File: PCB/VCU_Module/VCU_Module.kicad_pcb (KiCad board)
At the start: 2 copper layers, 85.2 x 107.8 mm, 66 parts, among them IC1 STM32C092RCT6, J1 5810132011, J10 12V, J11 Conn_ST_STDC14, J12 MCU1, J13 MCU2, J14 5V, J15 3V3, J16 MCU3, J17 MCU4, J2 CN1, J3 CN2, J4 CN3, J5 MCU6, J6 CN4, J7 MCU5, J8 Termination Resistor Jumper, J9 GND, Q1 PJD9P06A-AU_L2_000A1, SW2 SW_Push, U3 LMR33640DDDA, U4 LMR33640DDDA, U6 MCP2562FDT-H_SN

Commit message: move STLink connector and change component to correct version with alignment tabs
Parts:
- moved J11 41.0 mm to (156.0, 128.4), turned to 90 degrees
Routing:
- net /MCU/NRST: track 51.6 -> 68.6 mm, vias 1 -> 2
- net /MCU/VCP_RX: track 38.4 -> 25.9 mm
- net /MCU/VCP_TX: track 34.2 -> 24.2 mm
- net /MCU/SWCLK/BOOT0: track 34.1 -> 43.7 mm
- net /MCU/SWO: track 26.9 -> 35.6 mm
- net /MCU/SWDIO: track 35.0 -> 43.5 mm
- net 3V3: track 152.7 -> 150.8 mm

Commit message: move stdc14 connector reroute traces fix drc and schematic parity issues rerun make for build files
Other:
- board text added: "${TITLE} ${COMPANY} REV ${REVISION} ${ISSUE_DATE}"
- board text added: "CAN H CAN H CAN L CAN L"
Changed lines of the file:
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@@
 	(paper "A4")
 	(title_block
-		(title "BATTERY MANAGEMENT UNIT (BMU)")
-		(date "2026-05-14")
+		(title "VEHICLE CONTROL UNIT (VCU) Dev Board")
+		(date "2026-08-13")
 		(rev "1.0")
 		(company "VIKING MOTOR SPORTS (VMS)")
@@
 		(sheetname "/MCU/")
 		(sheetfile "MCU.kicad_sch")
+		(units
+			(unit
+				(name "A")
+				(pins "1" "4" "8" "2" "3" "5" "6" "7")
+			)
+		)
 		(attr smd)
 		(duplicate_pad_numbers_are_jumpers no)
@@
 		(sheetname "/")
 		(sheetfile "VCU_Module.kicad_sch")
+		(units
+			(unit
+				(name "A")
+				(pins "2" "3" "6" "1" "9" "7" "8" "5" "4")
+			)
+		)
 		(attr smd)
 		(duplicate_pad_numbers_are_jumpers no)
@@
 		)
 		(property "Value" "3V3"
-			(at 0 10 0)
-			(layer "F.Fab")
+			(at 3.1 4.31 0)
+			(layer "F.SilkS")
 			(effects
 				(font
@@
 		)
 		(property "Value" "5V"
-			(at 0 10 0)
-			(layer "F.Fab")
+			(at 2.85 3.21 0)
+			(layer "F.SilkS")
 			(effects
 				(font
@@
 			)
 		)
-		(property "Datasheet" "https://www.st.com/content/ccc/resource/technical/document/user_manual/group1/99/49/91/b6/b2/3a/46/e5/DM00526767/files/DM00526767.pdf/jcr:content/translations/en.DM00526767.pdf"
+		(property "Datasheet" "https://suddendocs.samtec.com/catalog_english/ftsh_th.pdf"
 			(at 0 0 90)
 			(layer "F.Fab")
@@
 			)
 		)
-		(property "DPN" "612-FTSH-107-01-F-DV-K-ND"
+		(property "DPN" "SAM12420-ND"
 			(at 0 0 90)
 			(unlocked yes)
@@
 			)
 		)
-		(property "MPN" "FTSH-107-01-F-DV-K"
+		(property "MPN" "FTSH-107-01-S-D-K"
 			(at 0 0 90)
 			(unlocked yes)
@@
 			)
 		)
-		(property "Purchase Link" "https://www.digikey.com/en/products/detail/samtec-inc/FTSH-107-01-F-DV-K/2650001"
+		(property "Purchase Link" "https://www.digikey.com/en/products/detail/samtec-inc/FTSH-107-01-S-D-K/2650004?gclsrc=aw.ds&gad_source=1&gad_campaignid=17336967819&gbraid=0AAAAADrbLlicyKK0eY_V0wleFKoDjVbWz&gclid=CjwKCAjw1vXTBhB-EiwAEKr_k6pgiYkH2W21gU4f999biLNDO9FzNBRms_SrUikYiU-KfRn2oXJkshoCrk8QAvD_BwE"
 			(at 0 0 90)
 			(unlocked yes)
@@
 			)
 		)
+		(property "MFR" "Samtec Inc."
+			(at 0 0 90)
+			(unlocked yes)
+			(layer "F.Fab")
+			(hide yes)
+			(effects
+				(font
+					(size 1 1)
+					(thickness 0.15)
+				)
+			)
+		)
 		(property ki_fp_filters "PinHeader?2x07?P1.27mm*")
 		(sheetname "/MCU/")
 		(sheetfile "MCU.kicad_sch")
+		(units
+			(unit
+				(name "A")
+				(pins "1" "2" "11" "3" "5" "7" "12" "6" "4" "8" "10" "9" "13" "14")
+			)
+		)
 		(attr through_hole)
 		(duplicate_pad_numbers_are_jumpers no)
@@
 		(sheetname "/MCU/")
 		(sheetfile "MCU.kicad_sch")
+		(units
+			(unit
+				(name "A")
+				(pins "1" "2" "3")
+			)
+		)
 		(attr smd)
 		(duplicate_pad_numbers_are_jumpers no)
@@
 		(sheetname "/MCU/")
 		(sheetfile "MCU.kicad_sch")
+		(units
+			(unit
+				(name "A")
+				(pins "10" "11" "12" "6" "17" "18" "19" "20" "21" "22" "23" "24" "36"
+					"37" "42" "43" "44" "45" "46" "47" "50" "51" "52" "53" "54" "55" "56"
+					"40" "41" "7" "9" "8" "35" "34" "33" "32" "31" "30" "63" "62" "61" "60"
+					"59" "58" "57" "29" "28" "27" "5" "4" "3" "2" "1" "64" "49" "48" "39"
+					"38" "26" "25" "16" "15" "14" "13"
+				)
+			)
+		)
 		(attr smd)
 		(duplicate_pad_numbers_are_jumpers no)
@@
 		(sheetname "/")
 		(sheetfile "VCU_Module.kicad_sch")
+		(units
+			(unit
+				(name "A")
+				(pins "2" "3" "6" "1" "9" "7" "8" "5" "4")
+			)
+		)
 		(attr smd)
 		(duplicate_pad_numbers_are_jumpers no)
@@
 		(sheetname "/")
 		(sheetfile "VCU_Module.kicad_sch")
+		(units
+			(unit
+				(name "A")
+				(pins "1" "3" "2" "4")
+			)
+		)
 		(attr through_hole)
 		(duplicate_pad_numbers_are_jumpers no)
@@
 		(sheetname "/")
 		(sheetfile "VCU_Module.kicad_sch")
+		(units
+			(unit
+				(name "A")
+				(pins "1" "2")
+			)
+		)
 		(attr smd)
 		(duplicate_pad_numbers_are_jumpers no)
@@
 		(sheetname "/")
 		(sheetfile "VCU_Module.kicad_sch")
+		(units
+			(unit
+				(name "A")
+				(pins "A1" "A2" "A3" "A4" "A5" "A6" "A7" "A8" "A9" "A10" "A11" "A12"
+					"A13" "A14" "A15" "A16" "A17" "A18" "A19" "A20"
+				)
+			)
+			(unit
+				(name "B")
+				(pins "B1" "B2" "B3" "B4" "B5" "B6" "B7" "B8" "B9" "B10" "B11" "B12")
+			)
+		)
 		(attr through_hole)
 		(duplicate_pad_numbers_are_jumpers no)
@@
 		(layer "Edge.Cuts")
 	)
+	(gr_text "CAN H\n\nCAN H\n\nCAN L\n\nCAN L"
+		(at 146.5 130.6 0)
+		(layer "F.SilkS")
+		(effects
+			(font
+				(size 0.79 0.5)
+				(thickness 0.125)
+			)
+			(justify left bottom)
+		)
+	)
 	(gr_text "PC10\n\nPC11\n\nPC12\n\nPC13\n\nPC14\n\nPC15\n\nPC0\n\nPC1\n\nPC2\n\nPC3"
 		(at 157.25 120.25 0)
@@
 				(thickness 0.125)
 			)
+			(justify left bottom)
+		)
+	)
+	(gr_text "${TITLE}\n${COMPANY}\nREV ${REVISION}\n${ISSUE_DATE}"
+		(at 116.5 154.5 0)
+		(layer "F.SilkS")
+		(effects
+			(font
+				(size 1 1)
+				(thickness 0.125)
+			)

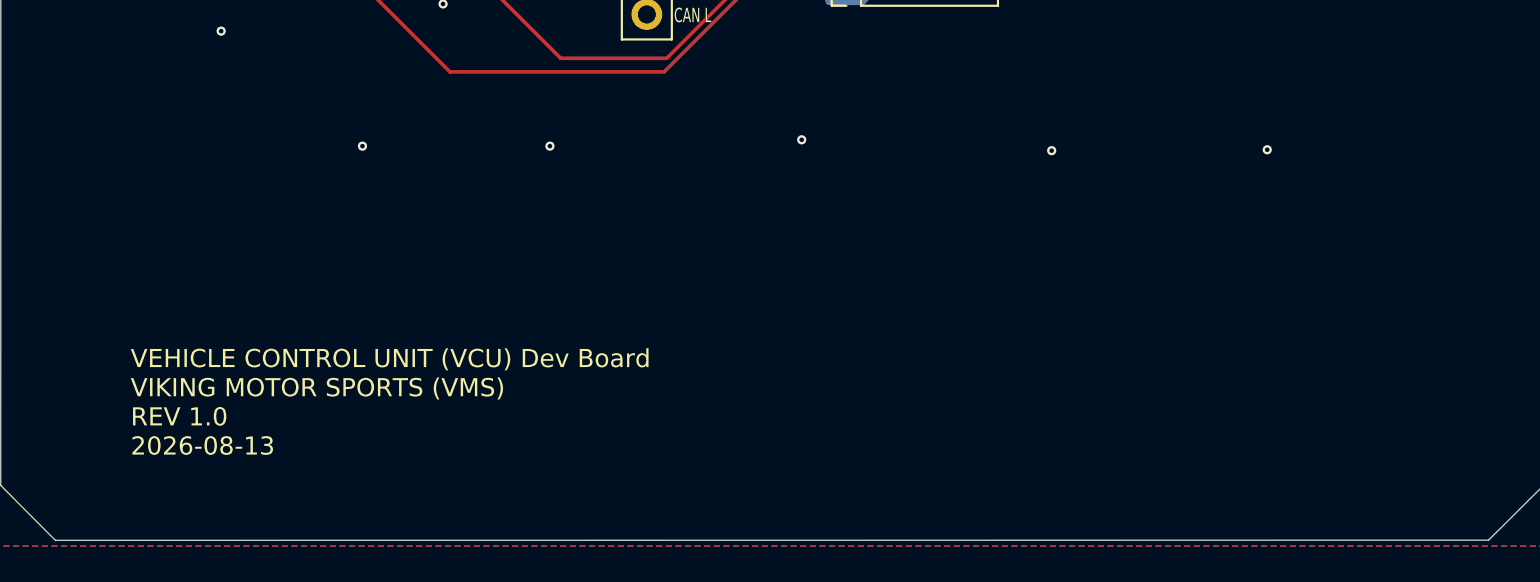
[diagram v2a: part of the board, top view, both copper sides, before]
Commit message: Add perfboard to allow placement of additional components
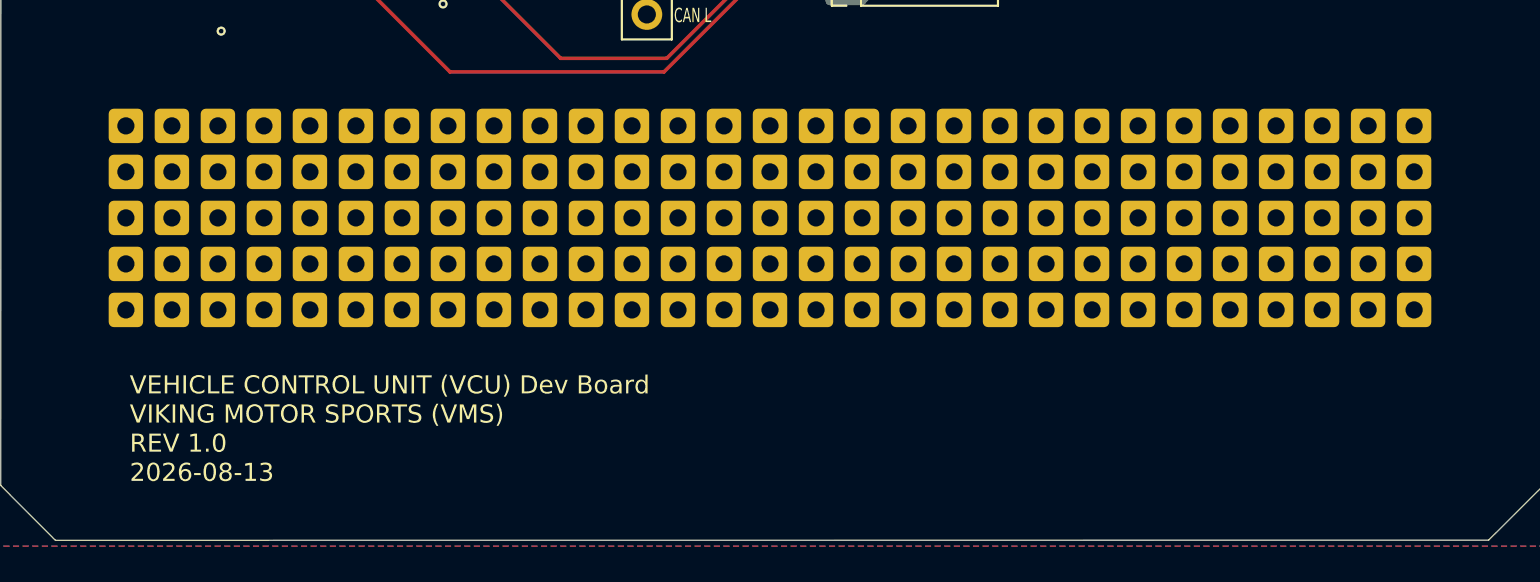
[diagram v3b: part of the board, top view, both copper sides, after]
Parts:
- added REF**: perf_hole, VMS_Footprints:perf_hole, F.Cu at (123.9, 136.2)
- added REF**: perf_hole, VMS_Footprints:perf_hole, F.Cu at (164.5, 138.8)
- added REF**: perf_hole, VMS_Footprints:perf_hole, F.Cu at (146.7, 146.4)
- added REF**: perf_hole, VMS_Footprints:perf_hole, F.Cu at (156.9, 143.9)
- added REF**: perf_hole, VMS_Footprints:perf_hole, F.Cu at (172.1, 136.2)
- added REF**: perf_hole, VMS_Footprints:perf_hole, F.Cu at (151.8, 136.2)
- added REF**: perf_hole, VMS_Footprints:perf_hole, F.Cu at (184.8, 136.2)
- added REF**: perf_hole, VMS_Footprints:perf_hole, F.Cu at (118.8, 143.9)
- added REF**: perf_hole, VMS_Footprints:perf_hole, F.Cu at (167.0, 146.4)
- added REF**: perf_hole, VMS_Footprints:perf_hole, F.Cu at (164.5, 146.4)
- added REF**: perf_hole, VMS_Footprints:perf_hole, F.Cu at (144.2, 136.2)
- added REF**: perf_hole, VMS_Footprints:perf_hole, F.Cu at (121.3, 136.2)
- added REF**: perf_hole, VMS_Footprints:perf_hole, F.Cu at (126.4, 138.8)
- added REF**: perf_hole, VMS_Footprints:perf_hole, F.Cu at (141.6, 146.4)
- added REF**: perf_hole, VMS_Footprints:perf_hole, F.Cu at (139.1, 141.3)
- added REF**: perf_hole, VMS_Footprints:perf_hole, F.Cu at (159.4, 143.9)
- added REF**: perf_hole, VMS_Footprints:perf_hole, F.Cu at (182.3, 146.4)
- added REF**: perf_hole, VMS_Footprints:perf_hole, F.Cu at (139.1, 138.8)
- added REF**: perf_hole, VMS_Footprints:perf_hole, F.Cu at (139.1, 146.4)
- added REF**: perf_hole, VMS_Footprints:perf_hole, F.Cu at (121.3, 141.3)
- added REF**: perf_hole, VMS_Footprints:perf_hole, F.Cu at (131.5, 146.4)
- added REF**: perf_hole, VMS_Footprints:perf_hole, F.Cu at (172.1, 143.9)
- added REF**: perf_hole, VMS_Footprints:perf_hole, F.Cu at (167.0, 143.9)
- added REF**: perf_hole, VMS_Footprints:perf_hole, F.Cu at (162.0, 141.3)
- added REF**: perf_hole, VMS_Footprints:perf_hole, F.Cu at (179.7, 138.8)
- added REF**: perf_hole, VMS_Footprints:perf_hole, F.Cu at (187.4, 143.9)
- added REF**: perf_hole, VMS_Footprints:perf_hole, F.Cu at (134.0, 146.4)
- added REF**: perf_hole, VMS_Footprints:perf_hole, F.Cu at (182.3, 143.9)
- added REF**: perf_hole, VMS_Footprints:perf_hole, F.Cu at (149.3, 136.2)
- added REF**: perf_hole, VMS_Footprints:perf_hole, F.Cu at (162.0, 138.8)
- added REF**: perf_hole, VMS_Footprints:perf_hole, F.Cu at (126.4, 141.3)
- added REF**: perf_hole, VMS_Footprints:perf_hole, F.Cu at (121.3, 146.4)
- added REF**: perf_hole, VMS_Footprints:perf_hole, F.Cu at (169.6, 141.3)
- added REF**: perf_hole, VMS_Footprints:perf_hole, F.Cu at (126.4, 136.2)
- added REF**: perf_hole, VMS_Footprints:perf_hole, F.Cu at (159.4, 138.8)
- added REF**: perf_hole, VMS_Footprints:perf_hole, F.Cu at (139.1, 143.9)
- added REF**: perf_hole, VMS_Footprints:perf_hole, F.Cu at (146.7, 141.3)
- added REF**: perf_hole, VMS_Footprints:perf_hole, F.Cu at (118.8, 141.3)
- added REF**: perf_hole, VMS_Footprints:perf_hole, F.Cu at (151.8, 141.3)
- added REF**: perf_hole, VMS_Footprints:perf_hole, F.Cu at (172.1, 138.8)
- added REF**: perf_hole, VMS_Footprints:perf_hole, F.Cu at (128.9, 141.3)
- added REF**: perf_hole, VMS_Footprints:perf_hole, F.Cu at (164.5, 141.3)
- added REF**: perf_hole, VMS_Footprints:perf_hole, F.Cu at (118.8, 146.4)
- added REF**: perf_hole, VMS_Footprints:perf_hole, F.Cu at (146.7, 136.2)
- added REF**: perf_hole, VMS_Footprints:perf_hole, F.Cu at (126.4, 143.9)
- added REF**: perf_hole, VMS_Footprints:perf_hole, F.Cu at (159.4, 146.4)
- added REF**: perf_hole, VMS_Footprints:perf_hole, F.Cu at (128.9, 146.4)
- added REF**: perf_hole, VMS_Footprints:perf_hole, F.Cu at (144.2, 138.8)
- added REF**: perf_hole, VMS_Footprints:perf_hole, F.Cu at (182.3, 138.8)
- added REF**: perf_hole, VMS_Footprints:perf_hole, F.Cu at (154.3, 143.9)
- added REF**: perf_hole, VMS_Footprints:perf_hole, F.Cu at (141.6, 136.2)
- added REF**: perf_hole, VMS_Footprints:perf_hole, F.Cu at (151.8, 143.9)
- added REF**: perf_hole, VMS_Footprints:perf_hole, F.Cu at (116.2, 146.4)
- added REF**: perf_hole, VMS_Footprints:perf_hole, F.Cu at (134.0, 143.9)
- added REF**: perf_hole, VMS_Footprints:perf_hole, F.Cu at (179.7, 141.3)
- added REF**: perf_hole, VMS_Footprints:perf_hole, F.Cu at (184.8, 138.8)
- added REF**: perf_hole, VMS_Footprints:perf_hole, F.Cu at (118.8, 136.2)
- added REF**: perf_hole, VMS_Footprints:perf_hole, F.Cu at (141.6, 141.3)
- added REF**: perf_hole, VMS_Footprints:perf_hole, F.Cu at (123.9, 146.4)
- added REF**: perf_hole, VMS_Footprints:perf_hole, F.Cu at (149.3, 141.3)
- added REF**: perf_hole, VMS_Footprints:perf_hole, F.Cu at (149.3, 146.4)
- added REF**: perf_hole, VMS_Footprints:perf_hole, F.Cu at (174.7, 138.8)
- added REF**: perf_hole, VMS_Footprints:perf_hole, F.Cu at (134.0, 136.2)
- added REF**: perf_hole, VMS_Footprints:perf_hole, F.Cu at (151.8, 138.8)
- added REF**: perf_hole, VMS_Footprints:perf_hole, F.Cu at (136.6, 146.4)
- added REF**: perf_hole, VMS_Footprints:perf_hole, F.Cu at (167.0, 141.3)
- added REF**: perf_hole, VMS_Footprints:perf_hole, F.Cu at (169.6, 136.2)
- added REF**: perf_hole, VMS_Footprints:perf_hole, F.Cu at (131.5, 136.2)
- added REF**: perf_hole, VMS_Footprints:perf_hole, F.Cu at (128.9, 143.9)
- added REF**: perf_hole, VMS_Footprints:perf_hole, F.Cu at (177.2, 141.3)
- added REF**: perf_hole, VMS_Footprints:perf_hole, F.Cu at (131.5, 143.9)
- added REF**: perf_hole, VMS_Footprints:perf_hole, F.Cu at (144.2, 141.3)
- added REF**: perf_hole, VMS_Footprints:perf_hole, F.Cu at (116.2, 136.2)
- added REF**: perf_hole, VMS_Footprints:perf_hole, F.Cu at (162.0, 143.9)
- added REF**: perf_hole, VMS_Footprints:perf_hole, F.Cu at (121.3, 143.9)
- added REF**: perf_hole, VMS_Footprints:perf_hole, F.Cu at (116.2, 138.8)
- added REF**: perf_hole, VMS_Footprints:perf_hole, F.Cu at (156.9, 141.3)
- added REF**: perf_hole, VMS_Footprints:perf_hole, F.Cu at (167.0, 136.2)
- added REF**: perf_hole, VMS_Footprints:perf_hole, F.Cu at (184.8, 141.3)
- added REF**: perf_hole, VMS_Footprints:perf_hole, F.Cu at (174.7, 141.3)
- added REF**: perf_hole, VMS_Footprints:perf_hole, F.Cu at (146.7, 138.8)
- added REF**: perf_hole, VMS_Footprints:perf_hole, F.Cu at (179.7, 146.4)
- added REF**: perf_hole, VMS_Footprints:perf_hole, F.Cu at (149.3, 138.8)
- added REF**: perf_hole, VMS_Footprints:perf_hole, F.Cu at (179.7, 136.2)
- added REF**: perf_hole, VMS_Footprints:perf_hole, F.Cu at (156.9, 136.2)
- added REF**: perf_hole, VMS_Footprints:perf_hole, F.Cu at (174.7, 143.9)
- added REF**: perf_hole, VMS_Footprints:perf_hole, F.Cu at (136.6, 141.3)
- added REF**: perf_hole, VMS_Footprints:perf_hole, F.Cu at (154.3, 141.3)
- added REF**: perf_hole, VMS_Footprints:perf_hole, F.Cu at (179.7, 143.9)
- added REF**: perf_hole, VMS_Footprints:perf_hole, F.Cu at (128.9, 136.2)
- added REF**: perf_hole, VMS_Footprints:perf_hole, F.Cu at (156.9, 146.4)
- added REF**: perf_hole, VMS_Footprints:perf_hole, F.Cu at (136.6, 138.8)
- added REF**: perf_hole, VMS_Footprints:perf_hole, F.Cu at (151.8, 146.4)
- added REF**: perf_hole, VMS_Footprints:perf_hole, F.Cu at (141.6, 143.9)
- added REF**: perf_hole, VMS_Footprints:perf_hole, F.Cu at (177.2, 143.9)
- added REF**: perf_hole, VMS_Footprints:perf_hole, F.Cu at (154.3, 138.8)
- added REF**: perf_hole, VMS_Footprints:perf_hole, F.Cu at (136.6, 136.2)
- added REF**: perf_hole, VMS_Footprints:perf_hole, F.Cu at (146.7, 143.9)
- added REF**: perf_hole, VMS_Footprints:perf_hole, F.Cu at (126.4, 146.4)
- added REF**: perf_hole, VMS_Footprints:perf_hole, F.Cu at (182.3, 136.2)
- added REF**: perf_hole, VMS_Footprints:perf_hole, F.Cu at (131.5, 138.8)
- added REF**: perf_hole, VMS_Footprints:perf_hole, F.Cu at (162.0, 146.4)
- added REF**: perf_hole, VMS_Footprints:perf_hole, F.Cu at (159.4, 136.2)
- added REF**: perf_hole, VMS_Footprints:perf_hole, F.Cu at (172.1, 141.3)
- added REF**: perf_hole, VMS_Footprints:perf_hole, F.Cu at (116.2, 141.3)
- added REF**: perf_hole, VMS_Footprints:perf_hole, F.Cu at (134.0, 138.8)
- added REF**: perf_hole, VMS_Footprints:perf_hole, F.Cu at (116.2, 143.9)
- added REF**: perf_hole, VMS_Footprints:perf_hole, F.Cu at (177.2, 146.4)
- added REF**: perf_hole, VMS_Footprints:perf_hole, F.Cu at (187.4, 138.8)
- added REF**: perf_hole, VMS_Footprints:perf_hole, F.Cu at (167.0, 138.8)
- added REF**: perf_hole, VMS_Footprints:perf_hole, F.Cu at (169.6, 138.8)
- added REF**: perf_hole, VMS_Footprints:perf_hole, F.Cu at (177.2, 138.8)
- added REF**: perf_hole, VMS_Footprints:perf_hole, F.Cu at (131.5, 141.3)
- added REF**: perf_hole, VMS_Footprints:perf_hole, F.Cu at (182.3, 141.3)
- added REF**: perf_hole, VMS_Footprints:perf_hole, F.Cu at (149.3, 143.9)
- added REF**: perf_hole, VMS_Footprints:perf_hole, F.Cu at (187.4, 146.4)
- added REF**: perf_hole, VMS_Footprints:perf_hole, F.Cu at (159.4, 141.3)
- added REF**: perf_hole, VMS_Footprints:perf_hole, F.Cu at (154.3, 146.4)
- added REF**: perf_hole, VMS_Footprints:perf_hole, F.Cu at (123.9, 143.9)
- added REF**: perf_hole, VMS_Footprints:perf_hole, F.Cu at (172.1, 146.4)
- added REF**: perf_hole, VMS_Footprints:perf_hole, F.Cu at (128.9, 138.8)
- added REF**: perf_hole, VMS_Footprints:perf_hole, F.Cu at (164.5, 136.2)
- added REF**: perf_hole, VMS_Footprints:perf_hole, F.Cu at (144.2, 146.4)
- added REF**: perf_hole, VMS_Footprints:perf_hole, F.Cu at (144.2, 143.9)
- added REF**: perf_hole, VMS_Footprints:perf_hole, F.Cu at (162.0, 136.2)
- added REF**: perf_hole, VMS_Footprints:perf_hole, F.Cu at (139.1, 136.2)
- added REF**: perf_hole, VMS_Footprints:perf_hole, F.Cu at (123.9, 141.3)
- added REF**: perf_hole, VMS_Footprints:perf_hole, F.Cu at (184.8, 143.9)
- added REF**: perf_hole, VMS_Footprints:perf_hole, F.Cu at (164.5, 143.9)
- added REF**: perf_hole, VMS_Footprints:perf_hole, F.Cu at (156.9, 138.8)
- added REF**: perf_hole, VMS_Footprints:perf_hole, F.Cu at (118.8, 138.8)
- added REF**: perf_hole, VMS_Footprints:perf_hole, F.Cu at (169.6, 146.4)
- added REF**: perf_hole, VMS_Footprints:perf_hole, F.Cu at (154.3, 136.2)
- added REF**: perf_hole, VMS_Footprints:perf_hole, F.Cu at (136.6, 143.9)
- added REF**: perf_hole, VMS_Footprints:perf_hole, F.Cu at (177.2, 136.2)
- added REF**: perf_hole, VMS_Footprints:perf_hole, F.Cu at (174.7, 136.2)
- added REF**: perf_hole, VMS_Footprints:perf_hole, F.Cu at (169.6, 143.9)
- added REF**: perf_hole, VMS_Footprints:perf_hole, F.Cu at (174.7, 146.4)
- added REF**: perf_hole, VMS_Footprints:perf_hole, F.Cu at (184.8, 146.4)
- added REF**: perf_hole, VMS_Footprints:perf_hole, F.Cu at (187.4, 141.3)
- added REF**: perf_hole, VMS_Footprints:perf_hole, F.Cu at (134.0, 141.3)
- added REF**: perf_hole, VMS_Footprints:perf_hole, F.Cu at (121.3, 138.8)
- added REF**: perf_hole, VMS_Footprints:perf_hole, F.Cu at (187.4, 136.2)
- added REF**: perf_hole, VMS_Footprints:perf_hole, F.Cu at (123.9, 138.8)
- added REF**: perf_hole, VMS_Footprints:perf_hole, F.Cu at (141.6, 138.8)
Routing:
- net GND: vias 121 -> 116

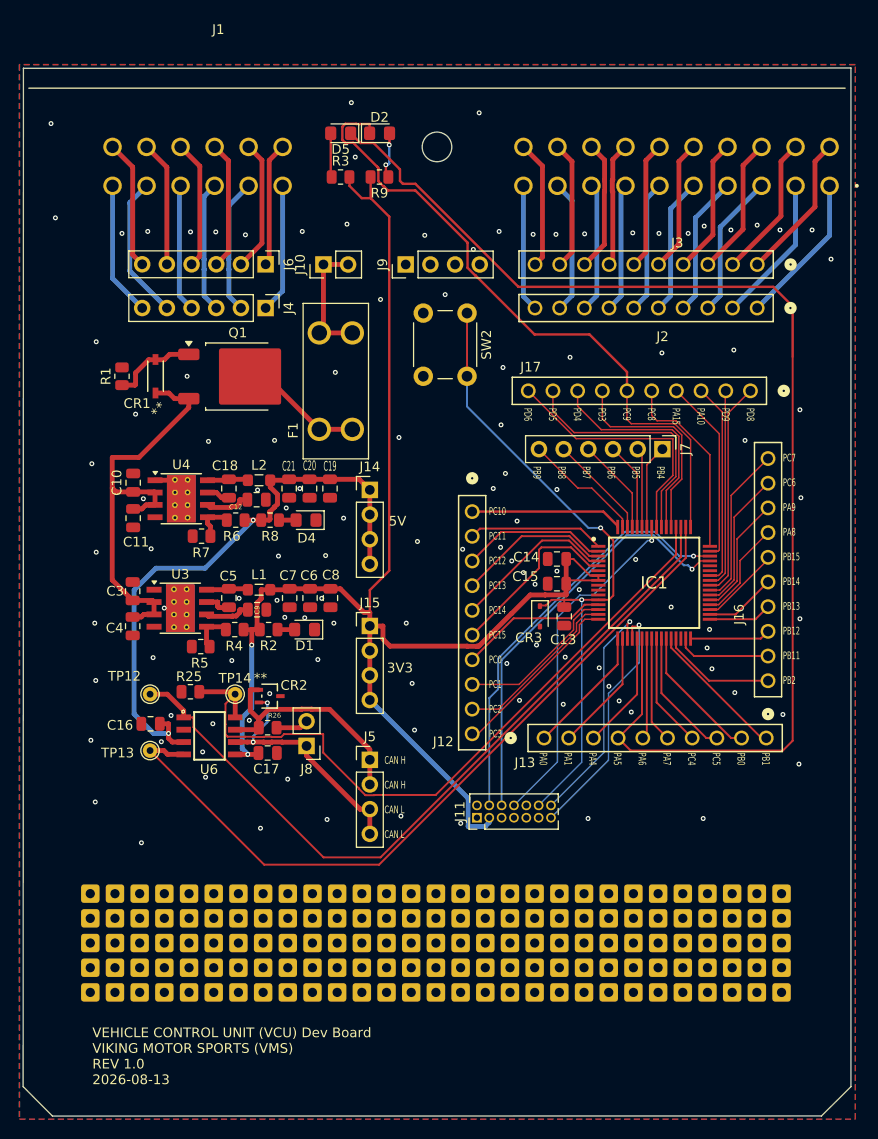
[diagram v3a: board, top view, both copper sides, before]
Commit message: Move CAN transceiver away from buck converters
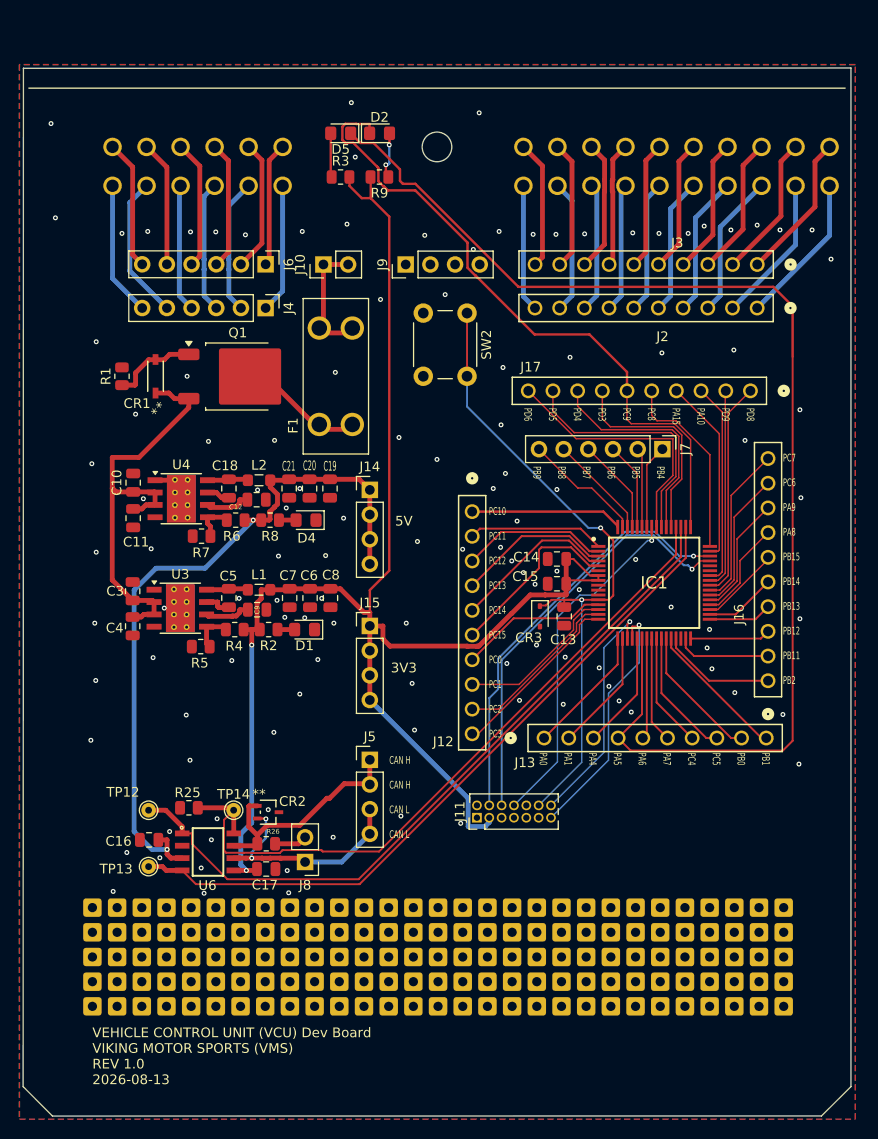
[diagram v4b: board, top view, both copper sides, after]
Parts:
- moved CR2 11.9 mm to (134.5, 127.8)
- moved J8 11.9 mm to (138.3, 133.0)
- moved R25 11.9 mm to (126.4, 127.4)
- moved R26 11.9 mm to (134.3, 131.1)
- moved TP12 11.9 mm to (122.2, 127.6)
- moved TP14 11.9 mm to (131.0, 127.6)
- moved U6 11.9 mm to (128.3, 131.9)
- moved C16 11.9 mm to (122.3, 130.7)
- moved C17 11.9 mm to (134.3, 133.7)
- moved TP13 11.9 mm to (122.2, 133.4)
- moved REF** 1.45 mm to (159.6, 145.3)
- moved REF** 1.45 mm to (187.6, 145.3)
- moved REF** 1.45 mm to (131.7, 145.3)
- moved REF** 1.45 mm to (141.9, 145.3)
- moved REF** 1.45 mm to (177.4, 145.3)
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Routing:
- net 3V3: track 150.8 -> 162.8 mm
- net 5V: track 62.1 -> 74.0 mm
- net /MCU/CAN_RXD: track 79.9 -> 73.1 mm
- net /MCU/CAN_TXD: track 78.5 -> 75.5 mm
- net /MCU/CANL: track 25.5 -> 23.6 mm
- net /MCU/STDBY: track 74.2 -> 73.1 mm
- net /MCU/CANH: track 24.8 -> 24.0 mm
- net GND: vias 116 -> 119
